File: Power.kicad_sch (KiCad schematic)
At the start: 27 parts, among them J10 Bus_PCI_Express_x1, J11 Conn_02x03_Odd_Even, J12 USB_C_Receptacle_PowerOnly_6P, J13 Conn_02x03_Odd_Even, J14 ATX-24, J15 Conn_01x02, J16 20V 5A DC, J17 8730, SW1 SW_Push

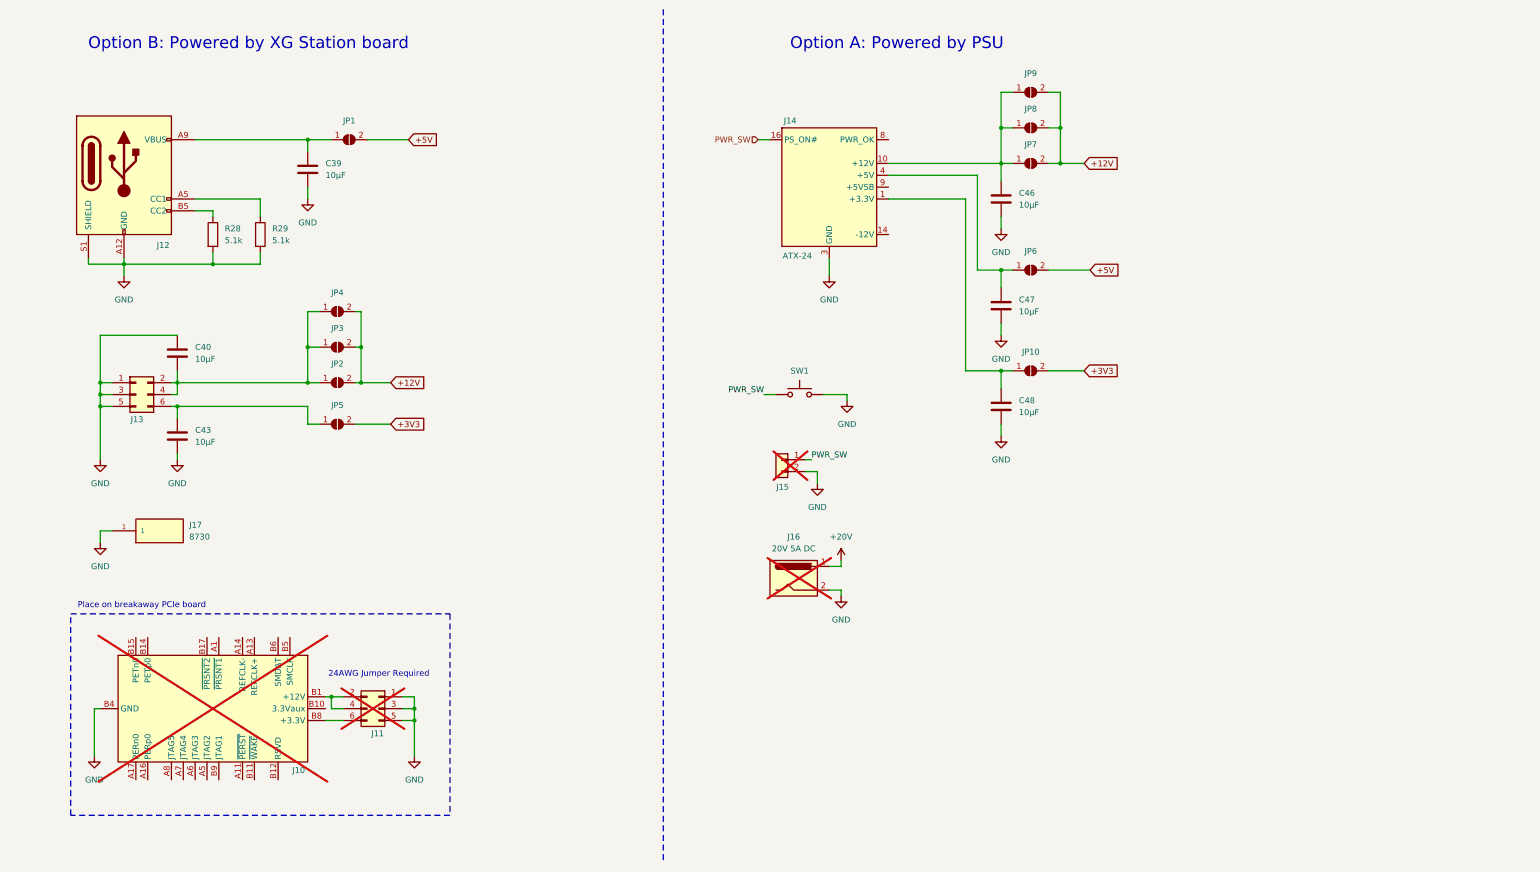
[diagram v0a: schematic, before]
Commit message: new power blocks
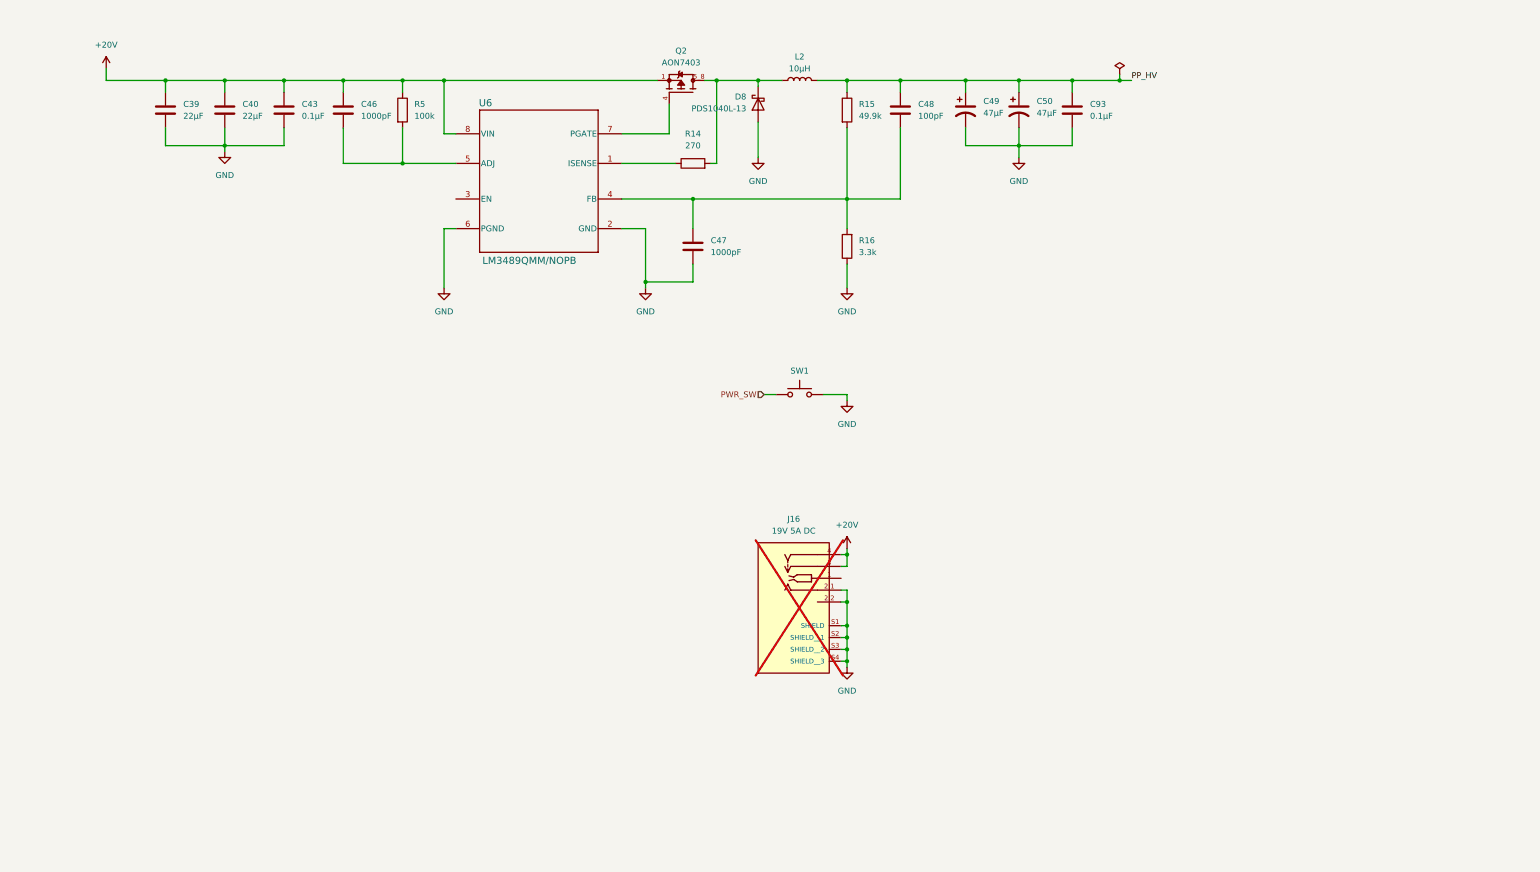
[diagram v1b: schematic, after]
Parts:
- removed J10: Bus_PCI_Express_x1, Connector_PCBEdge:BUS_PCIexpress_x1, symbol Connector:Bus_PCI_Express_x1
- removed J11: Conn_02x03_Odd_Even, Connector_PinHeader_2.54mm:PinHeader_1x06_P2.54mm_Vertical, symbol Connector_Generic:Conn_02x03_Odd_Even
- removed J12: USB_C_Receptacle_PowerOnly_6P, USB-C-SMD_TYPE-C-24P-QT:USB-C-SMD_TYPE-C-24P-QT, symbol Connector:USB_C_Receptacle_PowerOnly_6P
- removed J13: Conn_02x03_Odd_Even, Connector_PinHeader_2.54mm:PinHeader_2x03_P2.54mm_Vertical, symbol Connector_Generic:Conn_02x03_Odd_Even
- removed J14: ATX-24, 1-1775099-3:1-1775099-3, symbol Connector:ATX-24
- removed J15: Conn_01x02, Connector_PinHeader_2.54mm:PinHeader_1x02_P2.54mm_Vertical, symbol Connector_Generic:Conn_01x02
- removed J17: 8730, KEYSTONE_8730:KEYSTONE_8730, symbol KEYSTONE_8730:8730
- removed JP1, JP10, JP2, JP3, JP4, JP5, JP6, JP7, JP8, JP9: SolderJumper_2_Open, Jumper:SolderJumper-2_P1.3mm_Open_TrianglePad1.0x1.5mm, symbol Jumper:SolderJumper_2_Open
- removed R28, R29: 5.1k, Resistor_SMD:R_0402_1005Metric, symbol Device:R
- added C49, C50: 47µF, Capacitor_Tantalum_SMD:CP_EIA-7343-43_Kemet-X, symbol Device:C_Polarized_US
- added C93: 0.1µF, Capacitor_SMD:C_0402_1005Metric, symbol Device:C
- added D8: PDS1040L-13, Diode_SMD:D_PowerDI-5, symbol Diode:PMEG4050EP
- added L2: 10µH, Inductor_SMD:L_Abracon_ASPI-0630LR, symbol Device:L
- added Q2: AON7403, AON7403:TRANS_AON7403, symbol AON7403:AON7403
- added R14: 270, Resistor_SMD:R_0603_1608Metric, symbol Device:R
- added R15: 49.9k, Resistor_SMD:R_0402_1005Metric, symbol Device:R
- added R16: 3.3k, Resistor_SMD:R_0402_1005Metric, symbol Device:R
- added R5: 100k, Resistor_SMD:R_0402_1005Metric, symbol Device:R
- added U6: LM3489QMM/NOPB, LM3489QMM-NOPB, symbol LM3489QMM-NOPB:LM3489QMM_NOPB
- C39, C40: value 10μF -> 22µF; LCSC C15850 -> C45783; Part_Number CL21A106KAYNNNE -> CL21A226MAQNNNE
- C43: value 10μF -> 0.1µF; footprint Capacitor_SMD:C_0805_2012Metric -> Capacitor_SMD:C_0402_1005Metric; LCSC C15850 -> C307331; Part_Number CL21A106KAYNNNE -> CL05B104KB54PNC
- C46, C47: value 10μF -> 1000pF; footprint Capacitor_SMD:C_0805_2012Metric -> Capacitor_SMD:C_0402_1005Metric; LCSC C15850 -> C1523; Part_Number CL21A106KAYNNNE -> 0402B102K500NT
- C48: value 10μF -> 100pF; footprint Capacitor_SMD:C_0805_2012Metric -> Capacitor_SMD:C_0402_1005Metric; LCSC C15850 -> C1546; Part_Number CL21A106KAYNNNE -> 0402CG101J500NT
- J16: value 20V 5A DC -> 19V 5A DC; footprint Connector_BarrelJack:BarrelJack_CUI_PJ-063AH_Horizontal -> PJ-096H:CUI_PJ-096H; symbol Connector:Barrel_Jack -> PJ-096H:PJ-096H; LCSC C2928097 -> (none); MANUFACTURER (none) -> CUI; PARTREV (none) -> 1.0; Part_Number PJ-063AH -> PJ-096H; STANDARD (none) -> Manufacturer Recommendations
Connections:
- net +20V: now also C39.1, C40.1, C43.1, C46.1, J16.3, J16.4, Q2.1, R5.1, U6.8 (VIN); no longer J16.1
- net GND: now also C40.2, J16.2.1, J16.2.2, J16.S1 (SHIELD), J16.S2 (SHIELD__1), J16.S3 (SHIELD__2), J16.S4 (SHIELD__3), C49.2, C50.2, C93.2, D8.2 (A), R16.1, U6.2 (GND), U6.6 (PGND); no longer C40.1, C46.2, C48.2, J16.2
- net PP_HV: now reaches C48.1
- net PP_HV: now also C49.1, C50.1, C93.1, L2.2, R15.1
- net at C47.1: now also C48.2, R15.2, R16.2, U6.4 (FB)
- new net: D8.1 (K), L2.1, Q2.5_8, R14.2
- new net: R14.1, U6.1 (ISENSE)
- new net: C46.2, R5.2, U6.5 (ADJ)
- new net: Q2.4, U6.7 (PGATE)
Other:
- note removed: "24AWG Jumper Required"
- note removed: "Option A: Powered by PSU"
- note removed: "Option B: Powered by XG Station board"
- note removed: "Place on breakaway PCIe board"

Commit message: Laid out components for power circuits
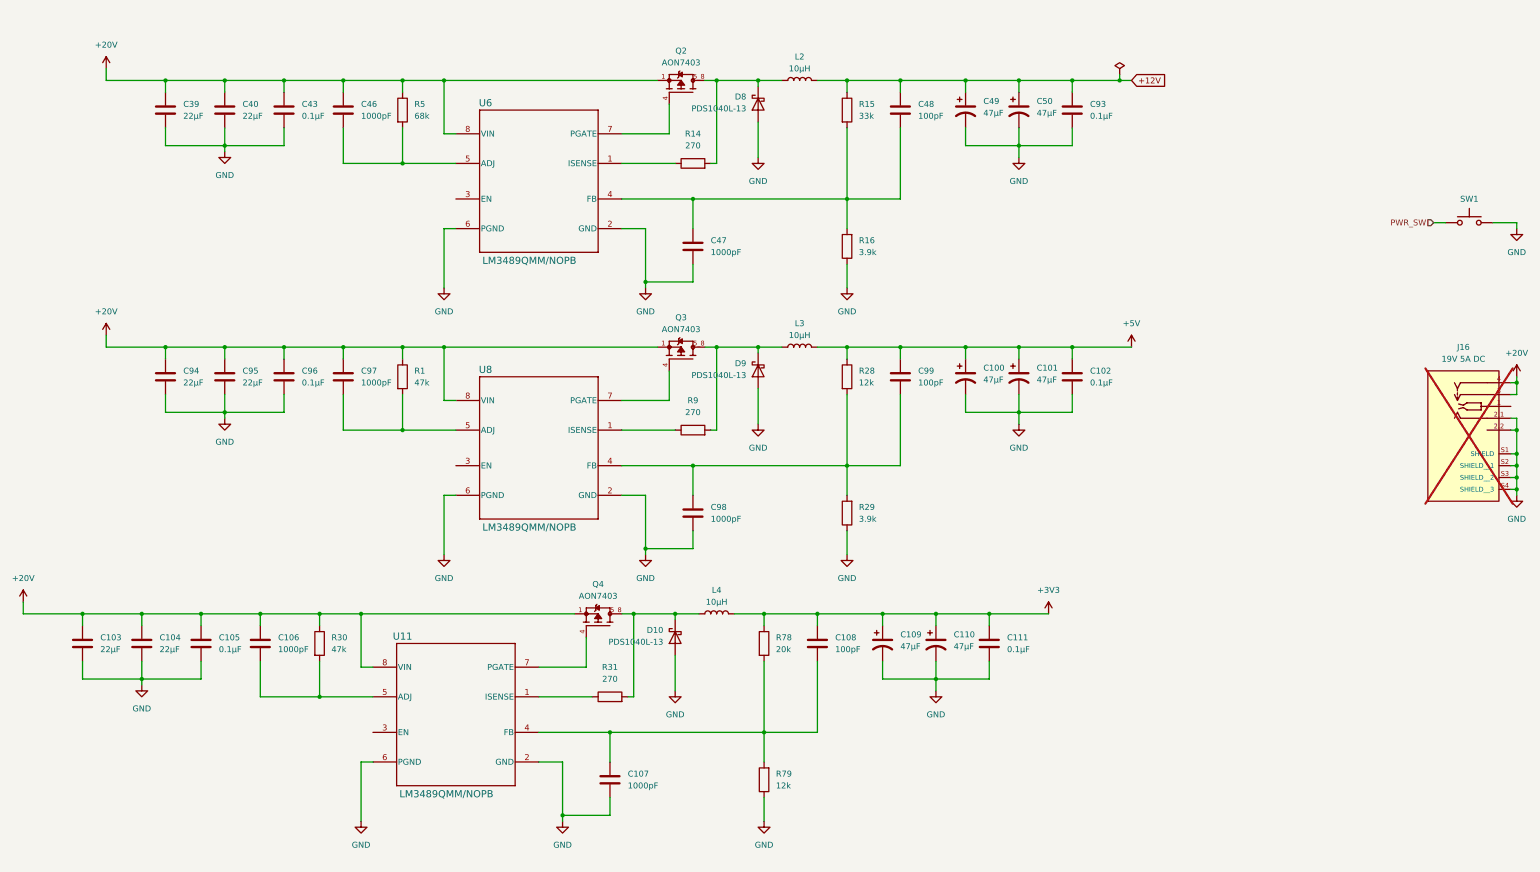
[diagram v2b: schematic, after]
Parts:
- added C100, C101, C109, C110: 47µF, Capacitor_Tantalum_SMD:CP_EIA-7343-43_Kemet-X, symbol Device:C_Polarized_US
- added C102, C105, C111, C96: 0.1µF, Capacitor_SMD:C_0402_1005Metric, symbol Device:C
- added C103, C104, C94, C95: 22µF, Capacitor_SMD:C_0805_2012Metric, symbol Device:C
- added C106, C107, C97, C98: 1000pF, Capacitor_SMD:C_0402_1005Metric, symbol Device:C
- added C108, C99: 100pF, Capacitor_SMD:C_0402_1005Metric, symbol Device:C
- added D10, D9: PDS1040L-13, Diode_SMD:D_PowerDI-5, symbol Diode:PMEG4050EP
- added L3, L4: 10µH, Inductor_SMD:L_Abracon_ASPI-0630LR, symbol Device:L
- added Q3, Q4: AON7403, AON7403:TRANS_AON7403, symbol AON7403:AON7403
- added R1, R30: 47k, Resistor_SMD:R_0402_1005Metric, symbol Device:R
- added R28, R79: 12k, Resistor_SMD:R_0402_1005Metric, symbol Device:R
- added R29: 3.9k, Resistor_SMD:R_0402_1005Metric, symbol Device:R
- added R31, R9: 270, Resistor_SMD:R_0603_1608Metric, symbol Device:R
- added R78: 20k, Resistor_SMD:R_0402_1005Metric, symbol Device:R
- added U11, U8: LM3489QMM/NOPB, LM3489QMM-NOPB, symbol LM3489QMM-NOPB:LM3489QMM_NOPB
- R15: value 49.9k -> 33k; LCSC C25897 -> C25779; Part_Number 0402WGF4992TCE -> 0402WGF3302TCE
- R16: value 3.3k -> 3.9k; LCSC C25890 -> C51721; Part_Number 0402WGF3301TCE -> 0402WGF3901TCE
- R5: value 100k -> 68k; LCSC C25741 -> C36871; Part_Number 0402WGF1003TCE -> 0402WGF6802TCE
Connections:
- net +20V: now also C103.1, C104.1, C105.1, C106.1, C94.1, C95.1, C96.1, C97.1, Q3.1, Q4.1, R1.1, R30.1, U11.8 (VIN), U8.8 (VIN)
- net GND: now also C100.2, C101.2, C102.2, C103.2, C104.2, C105.2, C107.2, C109.2, C110.2, C111.2, C94.2, C95.2, C96.2, C98.2, D10.2 (A), D9.2 (A), R29.1, R79.1, U11.2 (GND), U11.6 (PGND), U8.2 (GND), U8.6 (PGND)
- net PP_HV renamed +12V
- new net: C107.1, C108.2, R78.2, R79.2, U11.4 (FB)
- new net: R31.1, U11.1 (ISENSE)
- new net: D10.1 (K), L4.1, Q4.5_8, R31.2
- new net: C98.1, C99.2, R28.2, R29.2, U8.4 (FB)
- new net: D9.1 (K), L3.1, Q3.5_8, R9.2
- new net: C106.2, R30.2, U11.5 (ADJ)
- new net: Q3.4, U8.7 (PGATE)
- new net: Q4.4, U11.7 (PGATE)
- new net: R9.1, U8.1 (ISENSE)
- new net: C97.2, R1.2, U8.5 (ADJ)
- new net +3V3: C108.1, C109.1, C110.1, C111.1, L4.2, R78.1
- new net +5V: C100.1, C101.1, C102.1, C99.1, L3.2, R28.1
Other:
- moved on the sheet: J16, SW1
